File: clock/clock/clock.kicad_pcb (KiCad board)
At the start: 2 copper layers, 112.6 x 128.5 mm, 54 parts, among them J1 AVR-ISP, J10 Conn_01x07_Male, J11 CV_IN, J12 CLOCK_OUT, J13 SUBDIV_OUT, J2 EURORACK_CONN_10, J3 Conn_01x05_Female, J4 Conn_01x05_Male, J5 Conn_01x05_Female, J6 Conn_01x05_Male, J7 Conn_01x05_Female, J8 Conn_01x05_Male, J9 Conn_01x07_Female, SW1 SW_Push, SW2 SW_Push, SW3 Rotary_Encoder_Switch, U1 ATmega328P-PU, U2 L7805, U3 SM460281N, U4 SM460281N, U5 SM460281N, Y1 16MHz

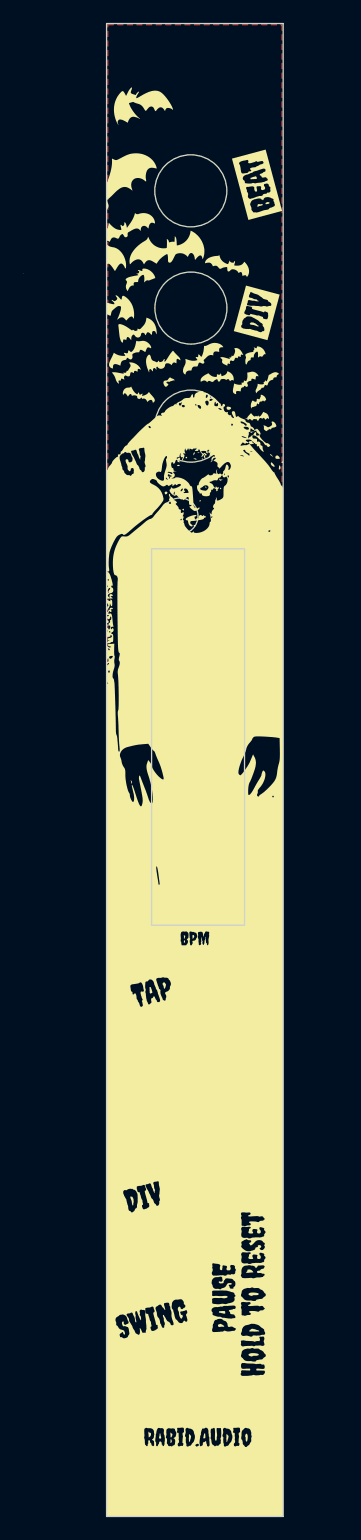
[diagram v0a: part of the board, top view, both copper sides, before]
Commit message: make ground plane connected, move LEDs wide
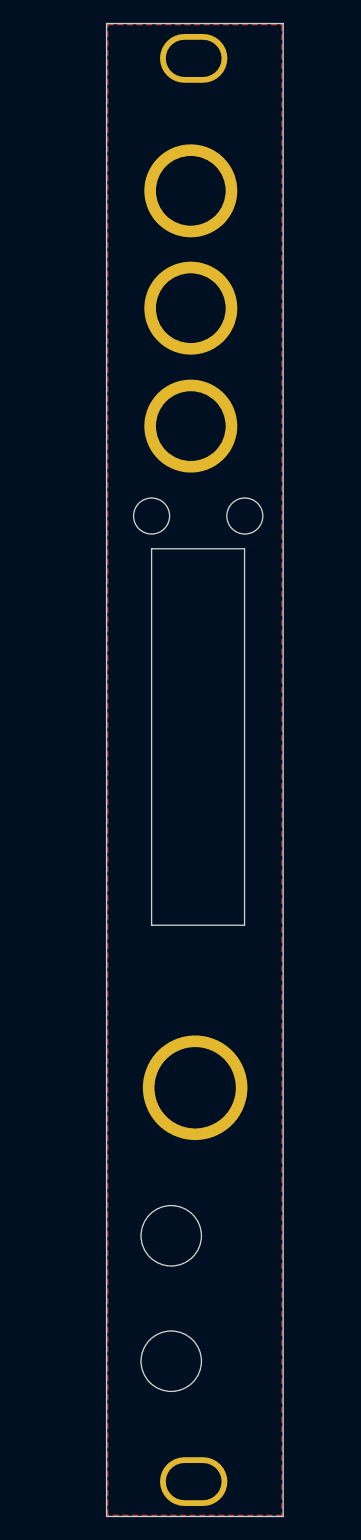
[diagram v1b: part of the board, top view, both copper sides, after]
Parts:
- removed HJ1 (x3): thonkiconn-hole, synth:thonkiconn_hole
- removed the REF** at (67.5, 185.5)
- removed the REF** at (67.5, 63.0)
- removed the REF** at (67.6, 151.6)
- added J14: SCREW1, synth:eurorack_screw_hole, F.Cu at (67.5, 63.0)
- added J15: BEAT_OUT, synth:thonkiconn_hole, F.Cu at (67.2, 74.4)
- added J16: DIV_OUT, synth:thonkiconn_hole, F.Cu at (67.2, 84.5)
- added J17: CV_IN, synth:thonkiconn_hole, F.Cu at (67.2, 94.7)
- added J18: KNOB, synth:knob_hole, F.Cu at (67.6, 151.6)
- added J19: SCREW2, synth:eurorack_screw_hole, F.Cu at (67.5, 185.5)
- J1: value AVR-ISP -> AVR-ISP-6
- J12: value CLOCK_OUT -> BEAT_OUT
- J13: value SUBDIV_OUT -> DIV_OUT
- moved REF** 2.44 mm to (63.9, 102.4)
- moved REF** 1.01 mm to (71.9, 102.4)
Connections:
- net /AGND renamed GND2
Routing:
- added copper zone on F.Cu, net GND1
- removed copper zone on F.Cu, net (none)
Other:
- board text added: "JLCJLCJLCJLC"

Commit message: back graphics
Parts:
- moved D2 1.10 mm to (152.2, 103.7)
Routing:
- net GND2: track 11.0 -> 6.39 mm
- net Net-(D2-Pad2): track 13.8 -> 14.4 mm
- net Net-(D1-Pad2): track 13.5 -> 14.1 mm
